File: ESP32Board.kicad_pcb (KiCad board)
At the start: 2 copper layers, 100 x 100 mm, 91 parts, among them J1 Conn_01x06_Pin, J2 USB_C_Receptacle_USB2.0_16P, Q1 BSS138, Q2 BSS138, U1 ESP32-WROOM-32E, U2 CH340K, U3 LF15_TO252

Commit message: ビア打ち
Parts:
- moved C7 15.3 mm to (180.6, 87.1)
- moved S1 11.3 mm to (204.1, 55.4), turned to 90 degrees
- moved C5 8.58 mm to (181.1, 97.1), turned to 180 degrees
- moved Q1 8.52 mm to (191.6, 50.0), turned to 0 degrees
- moved U3 7.79 mm to (176.7, 92.1), turned to 180 degrees
- moved Q2 6.03 mm to (191.6, 53.6)
- moved D3 5.50 mm to (170.4, 51.7)
- moved R4 5.50 mm to (173.7, 51.7)
- moved D5 5.45 mm to (170.4, 57.4)
- moved R6 5.45 mm to (173.8, 57.4)
- moved S2 4.12 mm to (204.0, 63.3), turned to 90 degrees
- moved R2 1.10 mm to (198.2, 109.3)
- moved D2 0.94 mm to (180.6, 99.6), turned to 180 degrees
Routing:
- net GND: track 0.00 -> 711.8 mm, vias 0 -> 452
- net +5V: track 47.5 -> 412.5 mm, vias 0 -> 1
- net /Neo: track 0.00 -> 81.0 mm, vias 0 -> 1
- net /EN: track 0.00 -> 66.3 mm, vias 0 -> 2
- net +3V3: track 0.00 -> 59.5 mm, vias 0 -> 3
- net /BOOT0: track 0.00 -> 34.6 mm
- net /RX1: track 0.00 -> 28.4 mm, vias 0 -> 1
- net /TX1: track 0.00 -> 25.5 mm, vias 0 -> 1
- net Net-(D1-A): track 0.00 -> 14.7 mm, vias 0 -> 2
- net /LED1: track 0.00 -> 13.4 mm, vias 0 -> 2
- net /RX0: track 0.00 -> 11.1 mm, vias 0 -> 2
- net Net-(Q1-S): track 0.00 -> 10.5 mm
- net Net-(Q1-G): track 0.00 -> 9.70 mm
- net /LED2: track 0.00 -> 8.91 mm, vias 0 -> 2
- net /LED3: track 0.00 -> 5.52 mm
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- added copper zone on B.Cu, net GND
- added copper zone on F.Cu, net GND

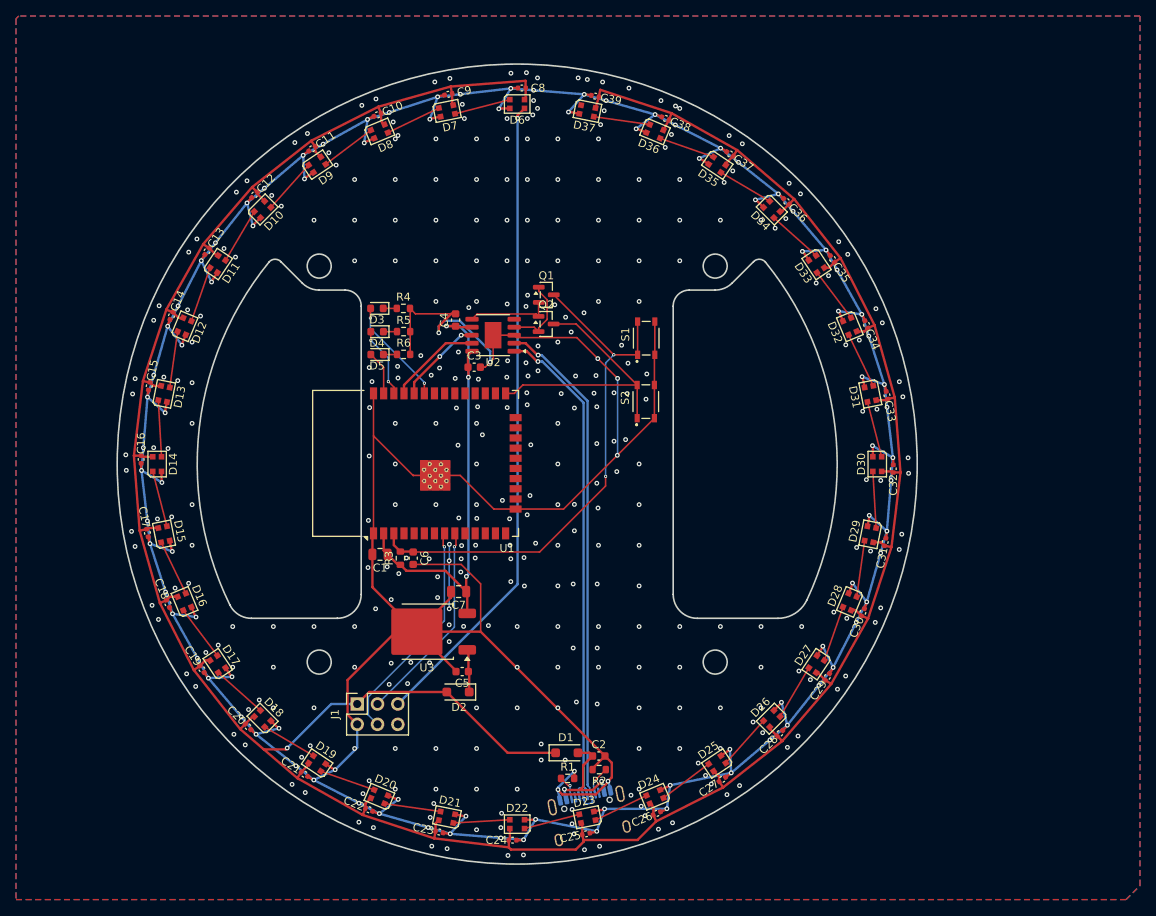
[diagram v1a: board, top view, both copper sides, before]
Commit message: シルク調整
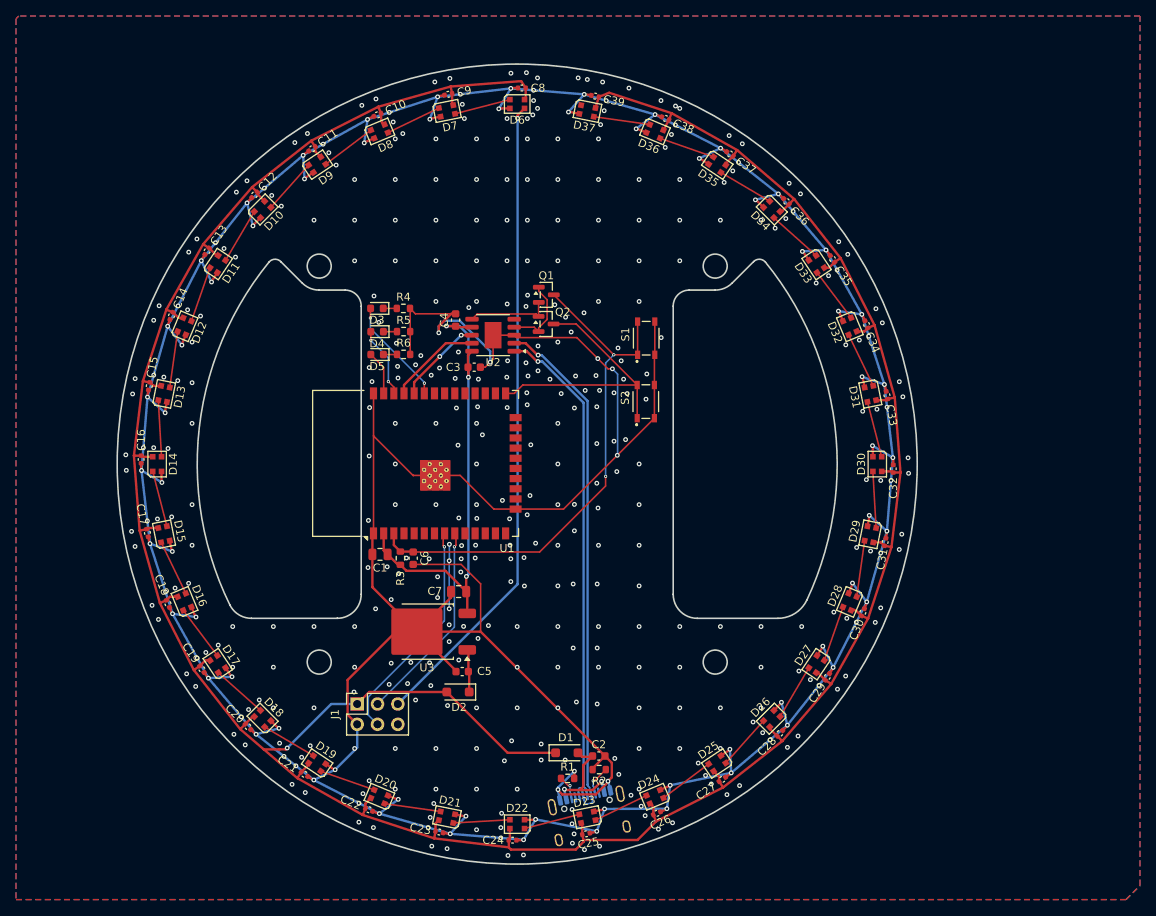
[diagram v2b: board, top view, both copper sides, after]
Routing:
- net +5V: track 412.5 -> 411.4 mm
- net GND: track 711.8 -> 712.2 mm, vias 452 -> 473

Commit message: ビアうち
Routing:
- net GND: track 712.2 -> 714.0 mm, vias 473 -> 481
- net Net-(D1-A): track 14.8 -> 15.7 mm
- net Net-(D22-DOUT): track 7.09 -> 7.60 mm

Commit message: なんか編集した
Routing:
- net GND: vias 481 -> 482
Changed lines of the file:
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@@
 	)
 	(via
-		(at 179.46 83.21)
+		(at 179.485 83.16)
 		(size 0.6)
 		(drill 0.3)
@@
 	)
 	(via
-		(at 189.06 51.41)
+		(at 189.685 51.785)
 		(size 0.6)
 		(drill 0.3)
@@
 	)
 	(via
+		(at 189.11 54.81)
+		(size 0.6)
+		(drill 0.3)
+		(layers "F.Cu" "B.Cu")
+		(free yes)
+		(net 2)
+	)
+	(via
 		(at 215.754566 111.309739)
 		(size 0.6)
@@
 	)
 	(via
-		(at 189.06 58.46)
+		(at 188.86 58.185)
 		(size 0.6)
 		(drill 0.3)
@@
 	)
 	(via
-		(at 195.11 79.46)
+		(at 195.485 78.66)
 		(size 0.6)
 		(drill 0.3)
@@
 	)
 	(via
-		(at 186.76 58.21)
+		(at 187.16 58.185)
 		(size 0.6)
 		(drill 0.3)
@@
 	)
 	(via
-		(at 189.31 60.11)
+		(at 188.86 60.26)
 		(size 0.6)
 		(drill 0.3)
@@
 	)
 	(segment
+		(start 179.485002 83.159998)
+		(end 179.485002 81.14476)
+		(width 0.2)
+		(layer "B.Cu")
+		(net 2)
+	)
+	(segment
 		(start 179.339346 55.01)
 		(end 178.459 54.129654)
@@
 	)
 	(segment
-		(start 179.46 83.21)
-		(end 179.46 89.21)
-		(width 0.2)
-		(layer "B.Cu")
-		(net 2)
-	)
-	(segment
 		(start 199.86 59.21)
 		(end 200.51 59.86)
@@
 	)
 	(segment
-		(start 179.485002 81.14476)
-		(end 179.485002 83.184998)
-		(width 0.2)
-		(layer "B.Cu")
-		(net 2)
-	)
-	(segment
 		(start 234.92 70.32)
 		(end 233.861605 61.17393)
@@
 	)
 	(segment
+		(start 179.485 83.16)
+		(end 179.46 83.185)
+		(width 0.2)
+		(layer "B.Cu")
+		(net 2)
+	)
+	(segment
 		(start 178.459 53.590346)
 		(end 178.840346 53.209)
@@
 	)
 	(segment
-		(start 179.485002 83.184998)
-		(end 179.46 83.21)
-		(width 0.2)
-		(layer "B.Cu")
-		(net 2)
-	)
-	(segment
 		(start 178.01393 25.218395)
 		(end 180.848 24.890433)
@@
 	)
 	(segment
+		(start 179.46 83.185)
+		(end 179.46 89.21)
+		(width 0.2)
+		(layer "B.Cu")
+		(net 2)
+	)
+	(segment
 		(start 231.039236 52.410082)
 		(end 226.561357 44.365246)
@@
 	)
 	(segment
+		(start 179.485 83.16)
+		(end 179.485002 83.159998)
+		(width 0.2)
+		(layer "B.Cu")
+		(net 2)
+	)
+	(segment
 		(start 180.385 54.01)
 		(end 180.26 53.885)
@@
 	)
 	(segment
-		(start 189.01 56.01)
+		(start 189.135 56.01)
 		(end 187.585 56.01)
 		(width 0.3)
@@
 	)
 	(via
-		(at 189.01 56.01)
+		(at 189.135 56.01)
 		(size 0.6)
 		(drill 0.3)
@@
 	)
 	(segment
-		(start 189.535 56.01)
-		(end 196.761 63.236)
-		(width 0.3)
-		(layer "B.Cu")
-		(net 16)
-	)
-	(segment
 		(start 197.26 113.485)
 		(end 197.385 113.335)
@@
 	)
 	(segment
-		(start 189.01 56.01)
-		(end 189.535 56.01)
+		(start 196.761 111.209)
+		(end 196.76 111.21)
 		(width 0.3)
 		(layer "B.Cu")
@@
 	)
 	(segment
-		(start 196.761 63.236)
-		(end 196.761 111.209)
+		(start 196.41 113.56)
+		(end 196.585 113.635)
+		(width 0.2)
+		(layer "B.Cu")
+		(net 16)
+	)
+	(segment
+		(start 189.535 56.01)
+		(end 196.761 63.236)
 		(width 0.3)
 		(layer "B.Cu")
@@
 	)
 	(segment
-		(start 196.41 113.56)
-		(end 196.585 113.635)
-		(width 0.2)
+		(start 196.761 63.236)
+		(end 196.761 111.209)
+		(width 0.3)
 		(layer "B.Cu")
 		(net 16)
 	)
 	(segment
-		(start 196.761 111.209)
-		(end 196.76 111.21)
+		(start 189.135 56.01)
+		(end 189.535 56.01)
 		(width 0.3)
 		(layer "B.Cu")
@@
 	)
 	(segment
-		(start 190.635 52.66)
-		(end 190.635 50.935)
+		(start 189.085 52.66)
+		(end 188.785001 52.360001)
 		(width 0.2)
 		(layer "F.Cu")
@@
 	)
 	(segment
-		(start 182.959999 52.360001)
-		(end 182.31 53.01)
+		(start 190.635 52.66)
+		(end 189.085 52.66)
 		(width 0.2)
 		(layer "F.Cu")
@@
 	(segment
 		(start 190.635 52.66)
-		(end 190.335001 52.360001)
+		(end 190.635 50.935)
 		(width 0.2)
 		(layer "F.Cu")
@@
 	)
 	(segment
-		(start 190.335001 52.360001)
+		(start 188.785001 52.360001)
 		(end 182.959999 52.360001)
 		(width 0.2)
@@
 	)
 	(segment
+		(start 182.959999 52.360001)
+		(end 182.31 53.01)
+		(width 0.2)
+		(layer "F.Cu")
+		(net 17)
+	)
+	(segment
 		(start 190.635 54.56)
 		(end 190.635 54.105532)
@@
 	)
 	(segment
-		(start 197.51 111.41)
-		(end 197.682638 112.295962)
+		(start 197.46 110.71)
+		(end 197.46 111.36)
 		(width 0.2)
 		(layer "B.Cu")
@@
 	)
 	(segment
-		(start 197.46 111.36)
-		(end 197.51 111.41)
+		(start 197.51 111.41)
+		(end 197.682638 112.295962)
 		(width 0.2)
 		(layer "B.Cu")
@@
 	)
 	(segment
-		(start 197.46 110.71)
-		(end 197.46 111.36)
+		(start 197.46 111.36)
+		(end 197.51 111.41)
 		(width 0.2)
 		(layer "B.Cu")
